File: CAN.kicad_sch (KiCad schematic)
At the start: 4 parts, among them U4 MCP2542FDxMF

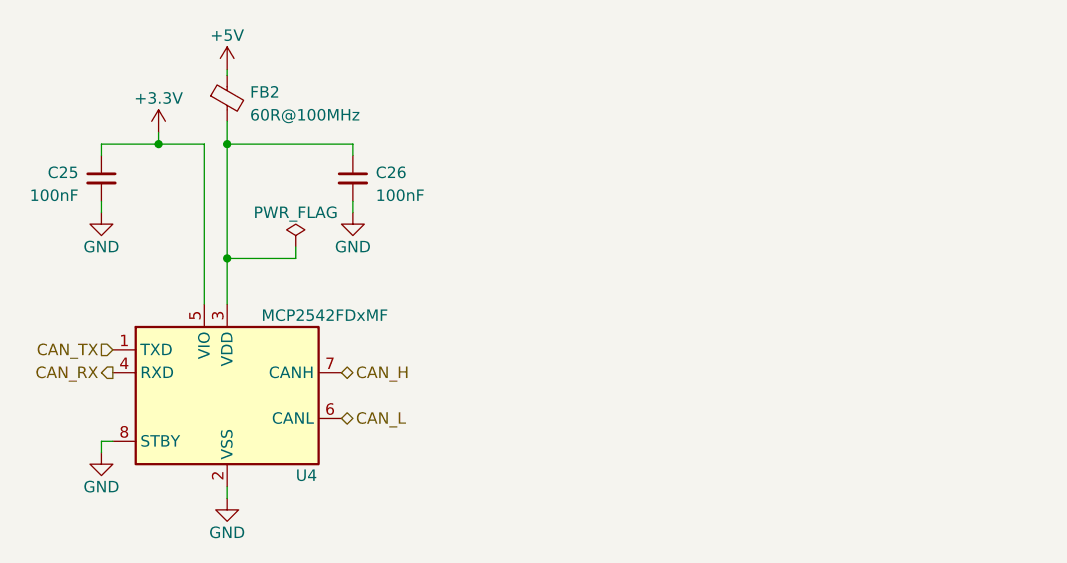
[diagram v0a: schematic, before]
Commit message: Finished schematic
Added UCB C connection
Added CAN
Power ICs schematic fixed
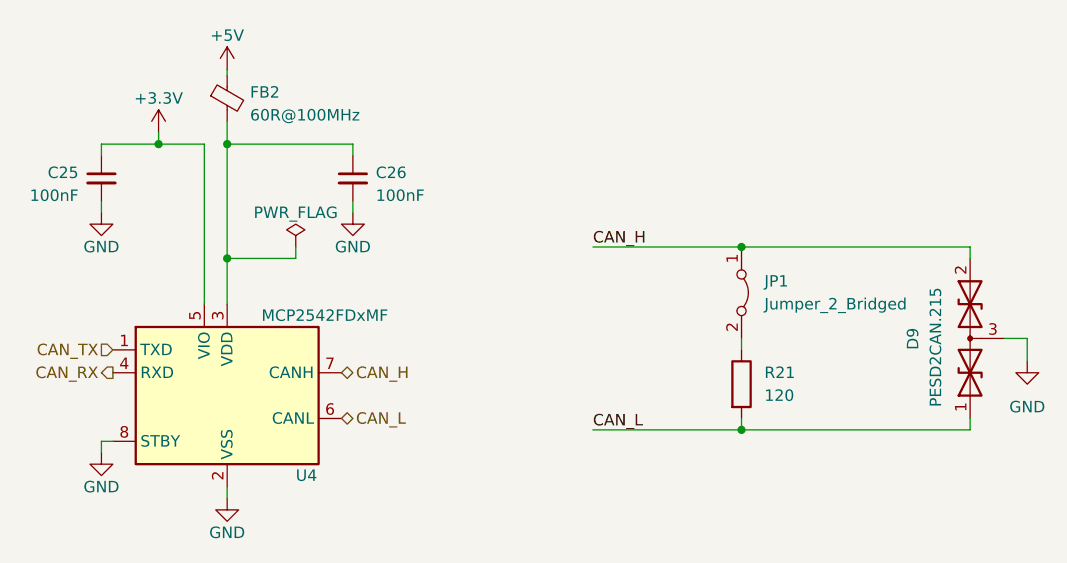
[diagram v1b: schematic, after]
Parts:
- added D9: PESD2CAN.215, Package_TO_SOT_SMD:SOT-23, symbol BMS_LV_2022-rescue:D_TVS_x2_AAC-Device
- added JP1: Jumper_2_Bridged, Connector_PinHeader_2.54mm:PinHeader_1x02_P2.54mm_Vertical, symbol Jumper:Jumper_2_Bridged
- added R21: 120, Resistor_SMD:R_0603_1608Metric, symbol Device:R
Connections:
- net CAN_H: now also D9.2 (A2), JP1.1 (A)
- net CAN_L: now also D9.1 (A1), R21.2
- net GND: now also D9.3 (common)
- new net: JP1.2 (B), R21.1

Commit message: Minor fixes
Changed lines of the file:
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@@
 	(wire
 		(pts
-			(xy 124.46 56.515) (xy 124.46 57.15)
+			(xy 124.46 55.88) (xy 124.46 57.15)
 		)
 		(stroke
@@
 	(symbol
 		(lib_id "power:+5V")
-		(at 124.46 56.515 0)
+		(at 124.46 55.88 0)
 		(unit 1)
 		(exclude_from_sim no)
@@
 		(fields_autoplaced yes)
 		(property "Reference" "#PWR033"
-			(at 124.46 60.325 0)
+			(at 124.46 59.69 0)
 			(effects
 				(font
@@
 		)
 		(property "Value" "+5V"
-			(at 124.46 52.705 0)
+			(at 124.46 52.07 0)
 			(effects
 				(font
@@
 		)
 		(property "Footprint" ""
-			(at 124.46 56.515 0)
+			(at 124.46 55.88 0)
 			(effects
 				(font
@@
 		)
 		(property "Datasheet" ""
-			(at 124.46 56.515 0)
+			(at 124.46 55.88 0)
 			(effects
 				(font
@@
 		)
 		(property "Description" ""
-			(at 124.46 56.515 0)
-			(effects
-				(font
+			(at 124.46 55.88 0)
+			(effects
+				(font

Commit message: Footprint changes + started PCB
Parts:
- C25, C26: footprint Capacitor_SMD:C_0402_1005Metric_Pad0.74x0.62mm_HandSolder -> Capacitor_SMD:C_0603_1608Metric_Pad1.08x0.95mm_HandSolder
- R21: footprint Resistor_SMD:R_0603_1608Metric -> Resistor_SMD:R_0603_1608Metric_Pad0.98x0.95mm_HandSolder
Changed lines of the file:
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@@
 			)
 		)
-		(property "Footprint" "Resistor_SMD:R_0603_1608Metric"
+		(property "Footprint" "Resistor_SMD:R_0603_1608Metric_Pad0.98x0.95mm_HandSolder"
 			(at 179.832 91.44 90)
 			(effects
@@
 			)
 		)
-		(property "Footprint" "Capacitor_SMD:C_0402_1005Metric_Pad0.74x0.62mm_HandSolder"
+		(property "Footprint" "Capacitor_SMD:C_0603_1608Metric_Pad1.08x0.95mm_HandSolder"
 			(at 110.49 68.58 0)
 			(effects
@@
 			)
 		)
-		(property "Footprint" "Capacitor_SMD:C_0402_1005Metric_Pad0.74x0.62mm_HandSolder"
+		(property "Footprint" "Capacitor_SMD:C_0603_1608Metric_Pad1.08x0.95mm_HandSolder"
 			(at 138.43 68.58 0)
 			(effects

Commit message: Minor changes
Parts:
- C25, C26: value 100nF -> 100n
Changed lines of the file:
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@@
 			)
 		)
-		(property "Value" "100nF"
+		(property "Value" "100n"
 			(at 107.95 70.4913 0)
 			(effects
@@
 		(fields_autoplaced yes)
 		(property "Reference" "C26"
-			(at 140.97 67.9513 0)
+			(at 140.97 67.3162 0)
 			(effects
 				(font
@@
 			)
 		)
-		(property "Value" "100nF"
-			(at 140.97 70.4913 0)
+		(property "Value" "100n"
+			(at 140.97 69.8562 0)
 			(effects
 				(font
